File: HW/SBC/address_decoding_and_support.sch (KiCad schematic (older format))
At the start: 8 parts, among them Q1 DS1813, SW1 RESET, U10 74LS138, U15 74LS74, U8 74HCT00, U9 74LS30, X1 8 MHz

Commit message: Connected most hierarchical labels between the sheets. Added a connector to AY IO port.
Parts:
- U15: footprint (none) -> Housings_DIP:DIP-14_W7.62mm_Socket
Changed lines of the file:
@@
 $EndComp
 $Comp
-L VCC #PWR35
+L VCC #PWR033
 U 1 1 58D6CEDE
 P 1875 4250
-F 0 "#PWR35" H 1875 4100 50  0001 C CNN
+F 0 "#PWR033" H 1875 4100 50  0001 C CNN
 F 1 "VCC" H 1875 4400 50  0000 C CNN
 F 2 "" H 1875 4250 50  0001 C CNN
@@
 $EndComp
 $Comp
-L GND #PWR36
+L GND #PWR034
 U 1 1 58D6CF02
 P 1875 5125
-F 0 "#PWR36" H 1875 4875 50  0001 C CNN
+F 0 "#PWR034" H 1875 4875 50  0001 C CNN
 F 1 "GND" H 1875 4975 50  0000 C CNN
 F 2 "" H 1875 5125 50  0001 C CNN
@@
 $EndComp
 $Comp
-L VCC #PWR37
+L VCC #PWR035
 U 1 1 58D6D2F3
 P 2075 3025
-F 0 "#PWR37" H 2075 2875 50  0001 C CNN
+F 0 "#PWR035" H 2075 2875 50  0001 C CNN
 F 1 "VCC" H 2075 3175 50  0000 C CNN
 F 2 "" H 2075 3025 50  0001 C CNN
@@
 $EndComp
 $Comp
-L GND #PWR34
+L GND #PWR036
 U 1 1 58D6D657
 P 1775 3400
-F 0 "#PWR34" H 1775 3150 50  0001 C CNN
+F 0 "#PWR036" H 1775 3150 50  0001 C CNN
 F 1 "GND" H 1775 3250 50  0000 C CNN
 F 2 "" H 1775 3400 50  0001 C CNN
@@
 $EndComp
 $Comp
-L VCC #PWR33
+L VCC #PWR037
 U 1 1 58D7E610
 P 1675 1100
-F 0 "#PWR33" H 1675 950 50  0001 C CNN
+F 0 "#PWR037" H 1675 950 50  0001 C CNN
 F 1 "VCC" H 1675 1250 50  0000 C CNN
 F 2 "" H 1675 1100 50  0001 C CNN
@@
 $EndComp
 $Comp
-L VCC #PWR38
+L VCC #PWR038
 U 1 1 58D83088
 P 6700 4725
-F 0 "#PWR38" H 6700 4575 50  0001 C CNN
+F 0 "#PWR038" H 6700 4575 50  0001 C CNN
 F 1 "VCC" H 6700 4875 50  0000 C CNN
 F 2 "" H 6700 4725 50  0001 C CNN
@@
 $EndComp
 $Comp
-L GND #PWR39
+L GND #PWR039
 U 1 1 58D830F6
 P 6700 4900
-F 0 "#PWR39" H 6700 4650 50  0001 C CNN
+F 0 "#PWR039" H 6700 4650 50  0001 C CNN
 F 1 "GND" H 6700 4750 50  0000 C CNN
 F 2 "" H 6700 4900 50  0001 C CNN
@@
 F 0 "U15" H 3175 4950 50  0000 C CNN
 F 1 "74LS74" H 3325 4355 50  0000 C CNN
-F 2 "" H 3025 4650 50  0001 C CNN
+F 2 "Housings_DIP:DIP-14_W7.62mm_Socket" H 3025 4650 50  0001 C CNN
 F 3 "" H 3025 4650 50  0001 C CNN
 	1    3025 4650

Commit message: Still no VCC net in PCBnew.
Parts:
- U10: footprint Housings_DIP:DIP-16_W7.62mm -> Housings_DIP:DIP-16_W7.62mm_Socket
- U8, U9: footprint Housings_DIP:DIP-14_W7.62mm -> Housings_DIP:DIP-14_W7.62mm_Socket
- X1: footprint Housings_DIP:DIP-8_W7.62mm -> Housings_DIP:DIP-8_W7.62mm_Socket
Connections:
- net VCC: no longer RN1.1 (common)
- net ~7F0X: no longer names the net of U10.15 (O0)
- net ~7F2X: no longer names the net of U10.14 (O1)
- net ~7F4X: no longer names the net of U10.13 (O2)
- new net Vcc: RN1.1 (common)
- no-connect marks 2 -> 5
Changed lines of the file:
@@
 EESchema Schematic File Version 2
-LIBS:pluto-rescue
 LIBS:power
 LIBS:device
@@
 LIBS:pluto
 LIBS:pluto-cache
-LIBS:IDE_interface-cache
 EELAYER 25 0
 EELAYER END
@@
 F 0 "U8" H 5450 2200 50  0000 C CNN
 F 1 "74HCT00" H 5450 2050 50  0000 C CNN
-F 2 "Housings_DIP:DIP-14_W7.62mm" H 5450 2150 50  0001 C CNN
+F 2 "Housings_DIP:DIP-14_W7.62mm_Socket" H 5450 2150 50  0001 C CNN
 F 3 "" H 5450 2150 50  0001 C CNN
 	1    5450 2150
@@
 F 0 "U8" H 8150 2650 50  0000 C CNN
 F 1 "74HCT00" H 8150 2500 50  0000 C CNN
-F 2 "Housings_DIP:DIP-14_W7.62mm" H 8150 2600 50  0001 C CNN
+F 2 "Housings_DIP:DIP-14_W7.62mm_Socket" H 8150 2600 50  0001 C CNN
 F 3 "" H 8150 2600 50  0001 C CNN
 	4    8150 2600
@@
 F 0 "U8" H 6250 1250 50  0000 C CNN
 F 1 "74HCT00" H 6250 1100 50  0000 C CNN
-F 2 "Housings_DIP:DIP-14_W7.62mm" H 6250 1200 50  0001 C CNN
+F 2 "Housings_DIP:DIP-14_W7.62mm_Socket" H 6250 1200 50  0001 C CNN
 F 3 "" H 6250 1200 50  0001 C CNN
 	2    6250 1200
@@
 F 0 "U8" H 7800 1725 50  0000 C CNN
 F 1 "74HCT00" H 7800 1575 50  0000 C CNN
-F 2 "Housings_DIP:DIP-14_W7.62mm" H 7800 1675 50  0001 C CNN
+F 2 "Housings_DIP:DIP-14_W7.62mm_Socket" H 7800 1675 50  0001 C CNN
 F 3 "" H 7800 1675 50  0001 C CNN
 	3    7800 1675
@@
 F 0 "U9" H 6950 3175 50  0000 C CNN
 F 1 "74LS30" H 6950 2975 50  0000 C CNN
-F 2 "Housings_DIP:DIP-14_W7.62mm" H 6950 3075 50  0001 C CNN
+F 2 "Housings_DIP:DIP-14_W7.62mm_Socket" H 6950 3075 50  0001 C CNN
 F 3 "" H 6950 3075 50  0001 C CNN
 	1    6950 3075
@@
 F 0 "U10" H 7725 5075 50  0000 C CNN
 F 1 "74LS138" H 8075 4026 50  0000 C CNN
-F 2 "Housings_DIP:DIP-16_W7.62mm" H 7925 4575 50  0001 C CNN
+F 2 "Housings_DIP:DIP-16_W7.62mm_Socket" H 7925 4575 50  0001 C CNN
 F 3 "" H 7925 4575 50  0001 C CNN
 	1    7925 4575
@@
 F 0 "X1" H 1675 4900 50  0000 L CNN
 F 1 "8 MHz" H 1925 4400 50  0000 L CNN
-F 2 "Housings_DIP:DIP-8_W7.62mm" H 2325 4300 50  0001 C CNN
+F 2 "Housings_DIP:DIP-8_W7.62mm_Socket" H 2325 4300 50  0001 C CNN
 F 3 "" H 1775 4650 50  0001 C CNN
 	1    1875 4650
@@
 $Comp
 L VCC #PWR037
-U 1 1 58D7E610
-P 1675 1100
-F 0 "#PWR037" H 1675 950 50  0001 C CNN
-F 1 "VCC" H 1675 1250 50  0000 C CNN
-F 2 "" H 1675 1100 50  0001 C CNN
-F 3 "" H 1675 1100 50  0001 C CNN
-	1    1675 1100
-	1    0    0    -1
-$EndComp
-$Comp
-L VCC #PWR038
 U 1 1 58D83088
 P 6700 4725
-F 0 "#PWR038" H 6700 4575 50  0001 C CNN
+F 0 "#PWR037" H 6700 4575 50  0001 C CNN
 F 1 "VCC" H 6700 4875 50  0000 C CNN
 F 2 "" H 6700 4725 50  0001 C CNN
@@
 $EndComp
 $Comp
-L GND #PWR039
+L GND #PWR038
 U 1 1 58D830F6
 P 6700 4900
-F 0 "#PWR039" H 6700 4650 50  0001 C CNN
+F 0 "#PWR038" H 6700 4650 50  0001 C CNN
 F 1 "GND" H 6700 4750 50  0000 C CNN
 F 2 "" H 6700 4900 50  0001 C CNN
@@
 Wire Wire Line
 	7325 4925 7025 4925
-Wire Wire Line
-	8525 4225 8650 4225
-Wire Wire Line
-	8650 4225 8650 3900
-Wire Wire Line
-	8650 3900 9125 3900
-Wire Wire Line
-	8525 4325 8700 4325
-Wire Wire Line
-	8700 4325 8700 4075
-Wire Wire Line
-	8700 4075 9125 4075
-Wire Wire Line
-	8525 4425 8750 4425
-Wire Wire Line
-	8750 4425 8750 4250
-Wire Wire Line
-	8750 4250 9125 4250
 Wire Wire Line
 	8525 4525 8825 4525
@@
 Text HLabel 2600 2650 2    60   Output ~ 0
 ~RES
-Text HLabel 9125 3900 2    60   Output ~ 0
-~7F0X
-Text HLabel 9125 4075 2    60   Output ~ 0
-~7F2X
-Text HLabel 9125 4250 2    60   Output ~ 0
-~7F4X
 Text HLabel 9125 4425 2    60   Output ~ 0
 ~7F6X
@@
 Text Label 4625 1775 0    60   ~ 0
 CLK
+NoConn ~ 8525 4425
+NoConn ~ 8525 4325
+NoConn ~ 8525 4225
+$Comp
+L Vcc #PWR039
+U 1 1 5938970E
+P 1675 1100
+F 0 "#PWR039" H 1675 1190 20  0001 C CNN
+F 1 "Vcc" H 1675 1190 30  0000 C CNN
+F 2 "" H 1675 1100 60  0000 C CNN
+F 3 "" H 1675 1100 60  0000 C CNN
+	1    1675 1100
+	1    0    0    -1
+$EndComp
 $EndSCHEMATC

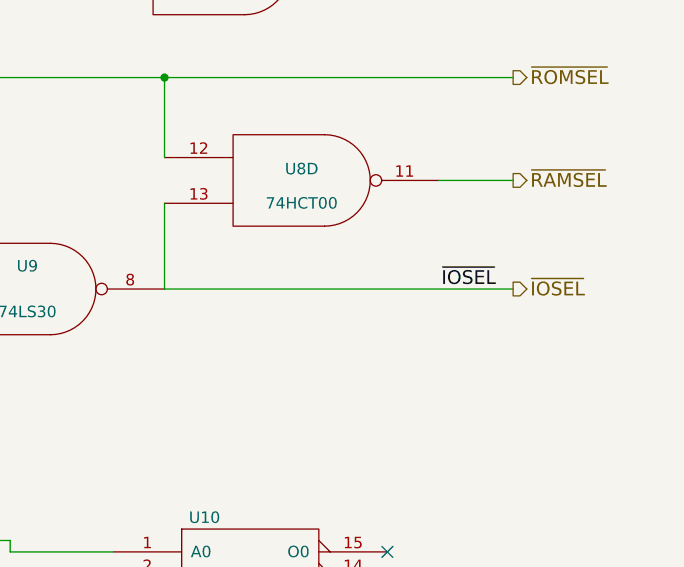
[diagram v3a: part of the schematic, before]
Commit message: New PCB layout. Added datasheet for AY-3-8912 and LM386.
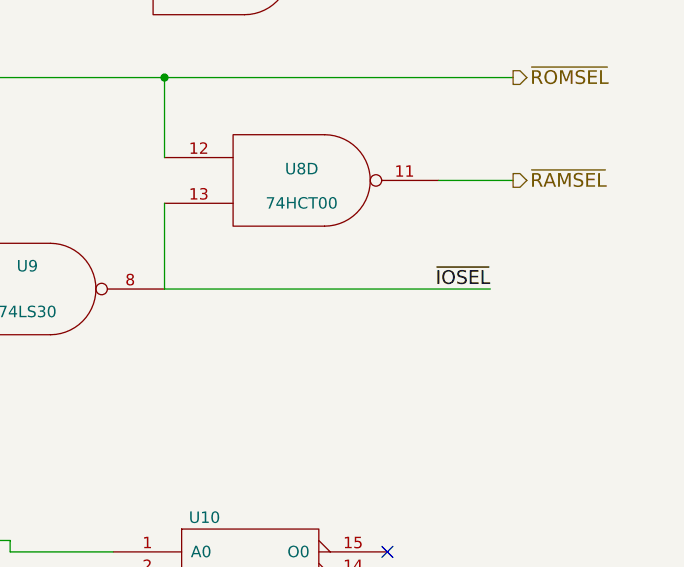
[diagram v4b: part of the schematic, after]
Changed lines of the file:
@@
 Connection ~ 7550 2150
 Wire Wire Line
-	7550 3075 9075 3075
+	7550 3075 8975 3075
 Wire Wire Line
 	7550 3075 7550 2700
@@
 Text HLabel 9075 2600 2    60   Output ~ 0
 ~RAMSEL
-Text Label 9000 3075 2    60   ~ 0
-~IOSEL
-Text HLabel 9075 3075 2    60   Output ~ 0
+Text Label 8975 3075 2    60   ~ 0
 ~IOSEL
 Text Label 6700 5100 0    60   ~ 0

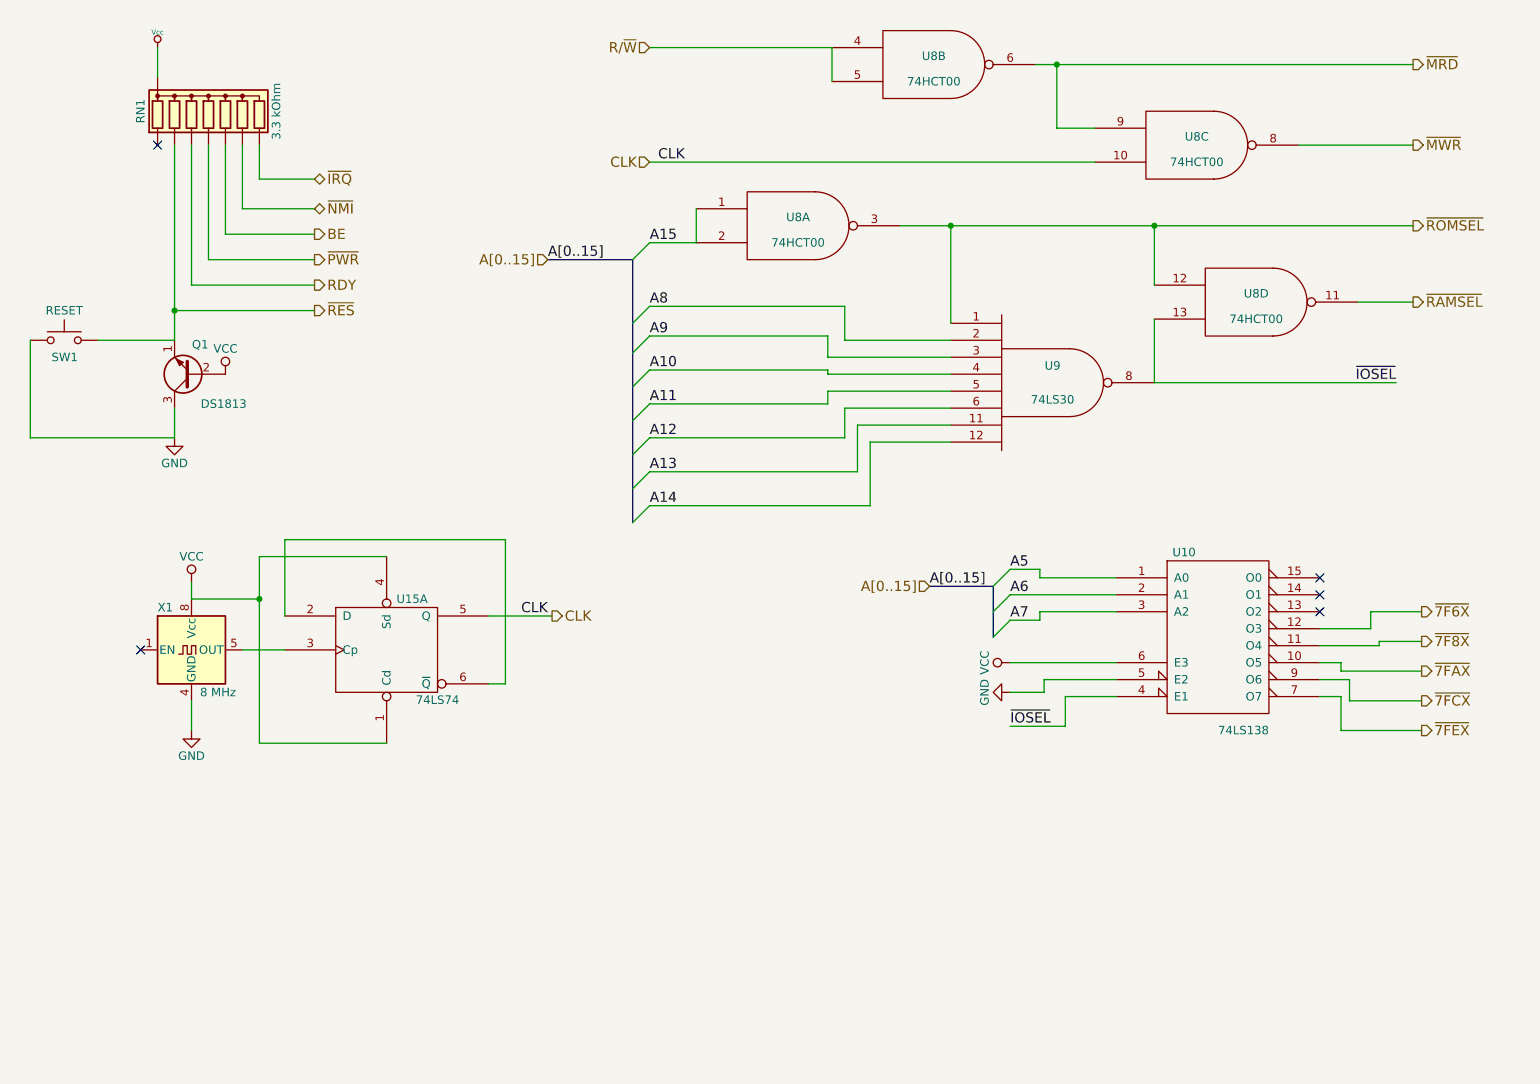
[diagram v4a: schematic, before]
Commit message: Schema is now Alpha.
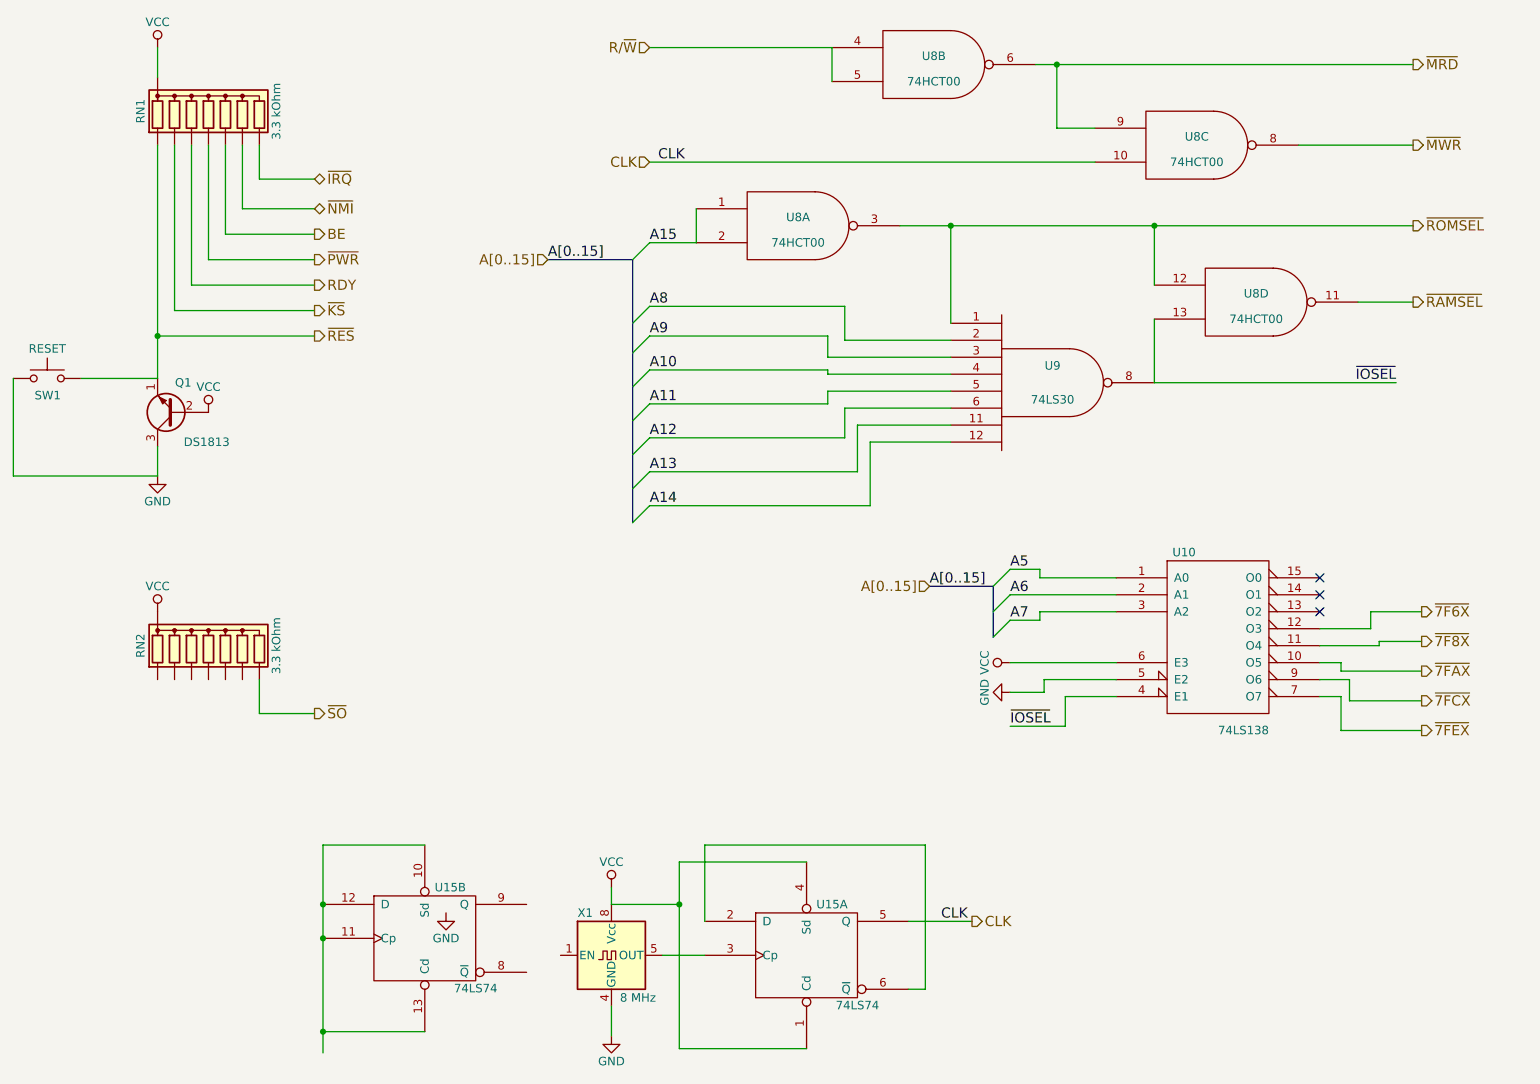
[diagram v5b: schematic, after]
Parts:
- added RN2: 3.3 kOhm, Resistors_THT:R_Array_SIP8, symbol R_Network07
- added unit 2 of U15
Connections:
- net Vcc is gone; now on net VCC: RN1.1 (common)
- net GND: now also U15.7 (GND)
- net VCC: now also RN2.1 (common), U15.14 (VCC)
- net ~RES: now also RN1.2 (R1); no longer RN1.3 (R2)
- new net: U15.10 (Sd), U15.11 (Cp), U15.12 (D), U15.13 (Cd)
- new net ~KS: RN1.3 (R2)
- new net ~SO: RN2.8 (R7)
- no-connect marks 5 -> 3
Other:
- moved on the sheet: Q1, SW1, U15A, X1
